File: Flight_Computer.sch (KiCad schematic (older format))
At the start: 138 parts, among them IC1 PIC32MZ2048EFH144-I_PL, IC2 FAN4010IL6X_F113, IC3 FAN4010IL6X_F113, J1 ICSP Programming, J2 SC_19-20, J3 UJ2-MBH-1-SMT-TR, J4 47219-2001, Q1 Q_NPN_BEC, Q2 Q_NPN_BEC, U1 STMPS2141STR, U2 STMPS2141STR, U3 BNO055, U4 SN65HVD1050D, U8 TXB0104PWR

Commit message: More additions
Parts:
- removed C1, C10, C11, C2, C3, C30, C33, C4, C5, C6, C7, C8, C9: 100n, Capacitor_SMD:C_0603_1608Metric, symbol Device:C_Small
- removed C12, C13: 100n, Capacitor_SMD:C_0402_1005Metric, symbol Device:C
- removed C14, C15: 22u, Capacitor_SMD:C_0805_2012Metric, symbol Device:C
- removed C18, C21, C22, C23, C26, C27, C35, C36, C41, C54, C55: 100n, Capacitor_SMD:C_0402_1005Metric, symbol Device:C_Small
- removed C19, C20, C24, C25, C34, C37, C44, C45, C46, C64, C65, C66, C67, C68, C69, C70: 1n, Capacitor_SMD:C_0402_1005Metric, symbol Device:C_Small
- removed C28, C29: 2.2u, Capacitor_SMD:C_0402_1005Metric, symbol Device:C_Small
- removed C31: 1n, Capacitor_SMD:C_0603_1608Metric, symbol Device:C_Small
- removed C32, C39, C40: 100p, Capacitor_SMD:C_0402_1005Metric, symbol Device:C_Small
- removed C47, C48, C49, C60, C61, C62, C63: 10n, Capacitor_SMD:C_0402_1005Metric, symbol Device:C_Small
- removed C50, C51, C52, C56, C57, C58, C59: 1u, Capacitor_SMD:C_0402_1005Metric, symbol Device:C_Small
- removed D1, D2: >8V, Diode_SMD:D_0805_2012Metric, symbol Device:D_TVS
- removed D3: D_TVS_x2_AAC, Package_TO_SOT_SMD:SOT-23, symbol Device:D_TVS_x2_AAC
- removed IC1: PIC32MZ2048EFH144-I_PL, QFP50P2200X2200X160-144N, symbol SamacSys_Parts:PIC32MZ2048EFH144-I_PL
- removed IC2, IC3: FAN4010IL6X_F113, 6-LEAD_MICROPAK, symbol FAN4010IL6X_F113:FAN4010IL6X_F113
- removed J1: ICSP Programming, Connector_PinHeader_2.54mm:PinHeader_1x05_P2.54mm_Vertical, symbol Connector_Generic:Conn_01x05
- removed J2: SC_19-20, MASA_Library:Stack_Connector_2019_2020, symbol MASA_Library:SC_19-20
- removed J3: UJ2-MBH-1-SMT-TR, digikey-footprints:USB_Mini_B_Female_UJ2-MBH-1-SMT-TR, symbol dk_USB-DVI-HDMI-Connectors:UJ2-MBH-1-SMT-TR
- removed J4: 47219-2001, 472192001, symbol MASA_Library:47219-2001
- removed L1: 4.7u, Capacitor_SMD:C_0805_2012Metric, symbol Device:L
- removed L10, L11, L5, L6, L7, L8, L9: 220n, Inductor_SMD:L_0402_1005Metric, symbol Device:L
- removed L2: 4.7u, Inductor_SMD:L_0805_2012Metric, symbol Device:L
- removed L3, L4: 2.2u, Inductor_SMD:L_0402_1005Metric, symbol Device:L
- removed Q1, Q2: Q_NPN_BEC, Package_TO_SOT_SMD:SOT-23, symbol Device:Q_NPN_BEC
- removed R1, R2: 100, Resistor_SMD:R_0805_2012Metric, symbol Device:R_Small_US
- removed R10, R9: 1, Resistor_SMD:R_0402_1005Metric, symbol Device:R_Small_US
- removed R11, R13, R14, R22, R23, R24, R28, R29, R30: 3.3, Resistor_SMD:R_0402_1005Metric, symbol Device:R_Small_US
- removed R12, R25: 1k, Resistor_SMD:R_0402_1005Metric, symbol Device:R_Small_US
- removed R15, R16, R18: 0, Resistor_SMD:R_0603_1608Metric, symbol Device:R_Small_US
- removed R17: 10k, Resistor_SMD:R_0603_1608Metric, symbol Device:R_Small_US
- removed R19, R20: 60, Resistor_SMD:R_0603_1608Metric, symbol Device:R_Small_US
- removed R26, R27, R31, R7, R8: 10k, Resistor_SMD:R_0402_1005Metric, symbol Device:R_Small_US
- removed R3: 10k, Resistor_SMD:R_0805_2012Metric, symbol Device:R_Small_US
- removed R32, R33: 3.3k, Resistor_SMD:R_0402_1005Metric, symbol Device:R_Small_US
- removed R34, R35: 220m, Resistor_SMD:R_0805_2012Metric, symbol Device:R_Small_US
- removed R4: 1k, Resistor_SMD:R_0805_2012Metric, symbol Device:R_Small_US
- removed R5, R6: NP, Resistor_SMD:R_0402_1005Metric, symbol Device:R_Small_US
- removed TMP1, TMP2: LM50CIM3X, Package_TO_SOT_SMD:SOT-23, symbol MASA_Library:LM50CIM3X
- removed TP1, TP10, TP2, TP3, TP4, TP5, TP6, TP7, TP8, TP9: T, TestPoint:TestPoint_Pad_1.0x1.0mm, symbol Connector:TestPoint
- removed U1, U2: STMPS2141STR, digikey-footprints:SOT-753, symbol dk_PMIC-Power-Distribution-Switches-Load-Drivers:STMPS2141STR
- removed U3: BNO055, digikey-footprints:LGA-28_5.2x3.8mm_BNO0055, symbol dk_Motion-Sensors-IMUs-Inertial-Measurement-Units:BNO055
- removed U4: SN65HVD1050D, Package_SO:SOIC-8_3.9x4.9mm_P1.27mm, symbol Interface_CAN_LIN:SN65HVD1050D
- removed U8: TXB0104PWR, digikey-footprints:TSSOP-14_W4.4mm, symbol dk_Logic-Translators-Level-Shifters:TXB0104PWR
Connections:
- net labels removed: !ENABLE_3V3, !ENABLE_5V, +3.3V, +3.3VP, +3V3, +5V, +5VP, 3V3_FAULT, 5V_FAULT, BNO_BL_IND, BNO_BL_LOAD, BNO_ENABLE, BNO_INT, BNO_RX, BNO_TX, CAN_H, CAN_L, CAN_RX, CAN_TX, GND, I_3V3, I_5V, MCLR, PGEC, PGED, SCK, SDI, SDI1, SDO, SD_CLK, SD_CS, SD_MISO, SD_MOSI, TCK, TDI, TDO, TMS, TSENSE_1, TSENSE_2, UART1_RX, UART1_TX, UART2_RX, UART2_TX, USB_3V3, USB_D+, USB_D-, USB_VBUS, VDD
- wire segments 342 -> 0
- no-connect marks 8 -> 0
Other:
- note removed: "Consider Seperating Analog and Digital Grounds / Voltages\n"
- note removed: "ENABLE_X are Active Low\n"
- note removed: "KEEP CLOSE TO PIC PINS"
- note removed: "Power Conditioning"
- note removed: "RX"
- note removed: "TX"
- note removed: "Use high ESR for polarized cap"

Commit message: Finished routing
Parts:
- added C1, C10, C11, C18, C2, C21, C22, C23, C26, C27, C3, C30, C33, C35, C36, C4, C41, C5, C54, C55, C6, C7, C8, C9: 100n, Capacitor_SMD:C_0402_1005Metric, symbol Device:C_Small
- added C12, C13: 100n, Capacitor_SMD:C_0402_1005Metric, symbol Device:C
- added C14, C15: 22u, Capacitor_SMD:C_0805_2012Metric, symbol Device:C
- added C19, C20, C24, C25, C31, C34, C37, C44, C45, C46, C64, C65, C66, C67, C68, C69, C70: 1n, Capacitor_SMD:C_0402_1005Metric, symbol Device:C_Small
- added C28, C29: 2.2u, Capacitor_SMD:C_0402_1005Metric, symbol Device:C_Small
- added C32, C39, C40: 100p, Capacitor_SMD:C_0402_1005Metric, symbol Device:C_Small
- added C47, C48, C49, C60, C61, C62, C63: 10n, Capacitor_SMD:C_0402_1005Metric, symbol Device:C_Small
- added C50, C51, C52, C56, C57, C58, C59: 1u, Capacitor_SMD:C_0402_1005Metric, symbol Device:C_Small
- added D1, D2: >8V, Diode_SMD:D_0805_2012Metric, symbol Device:D_TVS
- added D3: D_TVS_x2_AAC, Package_TO_SOT_SMD:SOT-23, symbol Device:D_TVS_x2_AAC
- added IC1: PIC32MZ2048EFH144-I_PL, QFP50P2200X2200X160-144N, symbol SamacSys_Parts:PIC32MZ2048EFH144-I_PL
- added IC2, IC3: FAN4010IL6X_F113, 6-LEAD_MICROPAK, symbol FAN4010IL6X_F113:FAN4010IL6X_F113
- added J1: ICSP Programming, Connector_PinHeader_2.54mm:PinHeader_1x05_P2.54mm_Vertical, symbol Connector_Generic:Conn_01x05
- added J2: SC_19-20, MASA_Library:Stack_Connector_2019_2020, symbol MASA_Library:SC_19-20
- added J3: UJ2-MBH-1-SMT-TR, digikey-footprints:USB_Mini_B_Female_UJ2-MBH-1-SMT-TR, symbol dk_USB-DVI-HDMI-Connectors:UJ2-MBH-1-SMT-TR
- added J4: 47219-2001, 472192001, symbol MASA_Library:47219-2001
- added L1: 4.7u, Capacitor_SMD:C_0805_2012Metric, symbol Device:L
- added L10, L11, L5, L6, L7, L8, L9: 220n, Inductor_SMD:L_0402_1005Metric, symbol Device:L
- added L2: 4.7u, Inductor_SMD:L_0805_2012Metric, symbol Device:L
- added L3, L4: 2.2u, Inductor_SMD:L_0402_1005Metric, symbol Device:L
- added Q1, Q2: Q_NPN_BEC, Package_TO_SOT_SMD:SOT-23, symbol Device:Q_NPN_BEC
- added R1, R2: 100, Resistor_SMD:R_0402_1005Metric, symbol Device:R_Small_US
- added R10, R9: 1, Resistor_SMD:R_0402_1005Metric, symbol Device:R_Small_US
- added R11, R13, R14, R22, R23, R24, R28, R29, R30: 3.3, Resistor_SMD:R_0402_1005Metric, symbol Device:R_Small_US
- added R12, R25, R4: 1k, Resistor_SMD:R_0402_1005Metric, symbol Device:R_Small_US
- added R15, R16, R18: 0, Resistor_SMD:R_0402_1005Metric, symbol Device:R_Small_US
- added R17, R26, R27, R3, R31, R7, R8: 10k, Resistor_SMD:R_0402_1005Metric, symbol Device:R_Small_US
- added R19, R20: 60, Resistor_SMD:R_0603_1608Metric, symbol Device:R_Small_US
- added R21, R32, R33, R36: 3.3k, Resistor_SMD:R_0402_1005Metric, symbol Device:R_Small_US
- added R34, R35: 220m, Resistor_SMD:R_0805_2012Metric, symbol Device:R_Small_US
- added R5, R6: NP, Resistor_SMD:R_0402_1005Metric, symbol Device:R_Small_US
- added TMP1, TMP2: LM50CIM3X, Package_TO_SOT_SMD:SOT-23, symbol MASA_Library:LM50CIM3X
- added TP1, TP10, TP2, TP3, TP4, TP5, TP6, TP7, TP8, TP9: T, TestPoint:TestPoint_Pad_1.0x1.0mm, symbol Connector:TestPoint
- added U1, U2: STMPS2141STR, digikey-footprints:SOT-753, symbol dk_PMIC-Power-Distribution-Switches-Load-Drivers:STMPS2141STR
- added U3: BNO055, digikey-footprints:LGA-28_5.2x3.8mm_BNO0055, symbol dk_Motion-Sensors-IMUs-Inertial-Measurement-Units:BNO055
- added U4: SN65HVD1050D, Package_SO:SOIC-8_3.9x4.9mm_P1.27mm, symbol Interface_CAN_LIN:SN65HVD1050D
- added U8: TXB0104PWR, digikey-footprints:TSSOP-14_W4.4mm, symbol dk_Logic-Translators-Level-Shifters:TXB0104PWR
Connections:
- new net: J1.4 (Pin_4), R1.2
- new net: J1.5 (Pin_5), R2.1
- new net: C2.2, R3.1, R4.2, TP1.1
- new net: C13.1, D2.2 (A2), L2.1, TP4.1, U2.1 (OUT)
- new net: R6.2, R8.2, U2.4 (EN)
- new net: C12.1, D1.2 (A2), L1.1, TP3.1, U1.1 (OUT)
- new net: C14.1, IC2.1 (VIN), L1.2, R34.1, TP5.1
- new net: C14.2, R9.2
- new net: R5.2, R7.2, U1.4 (EN)
- new net: C15.2, R10.2
- new net: Q2.3 (C), R27.1, U3.11 (RESET)
- new net: U3.19 (COM1), U8.13 (B1)
- new net: U3.20 (COM0), U8.12 (B2)
- new net: Q1.3 (C), R26.1, U3.4 (BOOT_LOAD)
- new net: C33.1, U3.9 (CAP)
- new net: C15.1, IC3.1 (VIN), L2.2, R35.1, TP6.1
- new net: C56.2, C60.2, J2.25 (UART1_TX), L8.2
- new net: C65.2, J2.27 (UART1_RX), L9.1
- new net: C58.2, C62.2, J2.29 (UART2_TX), L10.2
- new net: C67.2, J2.31 (UART2_RX), L11.1
- new net: C32.2, R15.2, U4.1 (TXD)
- new net: R16.2, U4.4 (RXD)
- new net: R18.1, U4.5 (VREF)
- new net: R17.2, U4.8 (S)
- new net: C22.2, C24.2, L3.1, R21.2, TMP1.2 (Vout)
- new net: C41.2, R18.2, R19.2, R20.1
- new net: C29.1, R14.1
- new net: C23.2, C25.2, L4.1, R36.2, TMP2.2 (Vout)
- new net: C50.1, R22.1
- new net: C51.1, R23.1
- new net: C52.1, R24.1
- new net: C54.1, Q1.1 (B), R12.1
- new net: C55.1, Q2.1 (B), R25.1
- new net: C28.1, R13.1
- new net: C56.1, R11.1
- new net: C57.1, R28.1
- new net: C58.1, R29.1
- new net: C59.1, R30.1
- new net !ENABLE_3V3: R5.1
- new net !ENABLE_5V: R6.1
- new net +3.3VP: J2.2 (3V3), J2.3 (3V3), J2.6 (3V3), J2.7 (3V3), U1.5 (IN)
- new net +3V3: C1.1, C10.2, C11.2, C3.1, C36.2, C37.2, C4.1, C5.1, C6.1, C69.2, C7.1, C8.1, C9.1, IC1.107 (VDD_6), IC1.122 (VDD_7), IC1.137 (VDD_8), IC1.18 (VDD_1), IC1.33 (VDD_2), IC1.41 (AVDD), IC1.55 (VDD_3), IC1.64 (VDD_4), IC1.88 (VDD_5), IC2.6 (LOAD), J1.2 (Pin_2), J4.4 (VDD), R3.2, R34.2, U8.1 (VCCA)
- new net +5V: C18.2, C19.1, C20.2, C21.1, C30.1, C31.1, C34.2, C35.2, C68.1, C70.1, IC3.6 (LOAD), R26.2, R27.2, R31.2, R35.2, TMP1.1 (Vs), TMP2.1 (Vs), U3.28 (VDDIO), U3.3 (VDD), U3.5 (PS1), U4.3 (VCC), U8.14 (VCCB), U8.8 (OE)
- new net +5VP: J2.34 (5V0), J2.35 (5V0), J2.38 (5V0), J2.39 (5V0), U2.5 (IN)
- new net 3V3_FAULT: U1.3 (FAULT)
- new net 5V_FAULT: U2.3 (FAULT)
- new net BNO_BL_IND: IC1.102 (RH14), U3.10 (BL_IND)
- new net BNO_BL_LOAD: IC1.101 (ERXDV/ECRSDV/RH13), R12.2
- new net BNO_ENABLE: IC1.100 (ECRS/RH12), R25.2
- new net BNO_INT: IC1.103 (EBIA23/RH15), U3.14 (INT)
- new net BNO_RX: IC1.91 (EBIA8/RPF5/SCL5/PMA8/RF5), U8.3 (A2)
- new net BNO_TX: IC1.90 (EBIA9/RPF4/SDA5/PMA9/RF4), U8.2 (A1)
- new net CAN_H: C39.2, D3.1 (A1), J2.21 (CAN_H), R19.1, TP9.1, U4.7 (CANH)
- new net CAN_L: C40.1, D3.2 (A2), J2.23 (CAN_L), R20.2, TP10.1, U4.6 (CANL)
- new net CAN_RX: IC1.105 (SOSCI/RPC13/RC13), R16.1, TP8.1
- new net CAN_TX: IC1.106 (SOSCO/RPC14/T1CK/RC14), R15.1, TP7.1
- new net GND: C1.2, C10.1, C11.1, C12.2, C13.2, C18.1, C19.2, C2.1, C20.1, C21.2, C22.1, C23.1, C24.1, C25.1, C26.1, C27.1, C3.2, C30.2, C31.2, C32.1, C33.2, C34.1, C35.1, C36.1, C37.1, C39.1, C4.2, C40.2, C41.1, C44.1, C45.1, C46.1, C47.1, C48.1, C49.1, C5.2, C54.2, C55.2, C6.2, C60.1, C61.1, C62.1, C63.1, C64.1, C65.1, C66.1, C67.1, C68.2, C69.1, C7.2, C70.2, C8.2, C9.2, D1.1 (A1), D2.1 (A1), D3.3 (common), IC1.108 (VSS_7), IC1.123 (VSS_8), IC1.136 (VSS_9), IC1.17 (VSS_1), IC1.32 (VSS_2), IC1.42 (AVSS), IC1.54 (VSS_3), IC1.63 (VSS_4), IC1.75 (VSS_5), IC1.89 (VSS_6), IC2.5 (GND), IC3.5 (GND), J1.3 (Pin_3), J2.1 (GND), J2.19 (GND), J2.20 (GND), J2.36 (GND), J2.37 (GND), J2.4 (GND), J2.40 (GND), J2.5 (GND), J3.5, J3.SH, J4.10 (GND_2), J4.11 (GND_3), J4.12 (GND_4), J4.6 (VSS), J4.9 (GND_1), Q1.2 (E), Q2.2 (E), R10.1, R11.2, R13.2, R14.2, R17.1, R21.1, R22.2, R23.2, R24.2, R28.2, R29.2, R30.2, R31.1, R32.1, R33.1, R36.1, R7.1, R8.1, R9.1, TMP1.3 (GND), TMP2.3 (GND), U1.2 (GND), U2.2 (GND), U3.15 (PIN15), U3.16 (PIN16), U3.17 (COM3), U3.18 (COM2), U3.2 (GND), U3.25 (GNDIO), U3.6 (PS0), U4.2 (GND), U8.7 (GND)
- new net I_3V3: IC1.66 (AN41/ERXD1/RH5), IC2.3 (IOUT), R32.2
- new net I_5V: IC1.65 (AN40/ERXERR/RH4), IC3.3 (IOUT), R33.2
- new net MCLR: IC1.20 (~MCLR), J1.1 (Pin_1), R4.1, TP2.1
- new net PGEC: IC1.35 (PGEC1/AN1/RPB1/RB1), R2.2
- new net PGED: IC1.36 (PGED1/AN0/RPB0/RB0), R1.1
- new net SCK: C46.2, IC1.109 (RPD1/SCK1/RD1), L7.1
- new net SDI: C48.2, C51.2, IC1.120 (ETXEN/RPD6/RD6), L6.2
- new net SDO: C44.2, IC1.110 (EBID14/RPD2/PMD14/RD2), L5.1
- new net SD_CLK: C49.2, C52.2, J4.5 (CLK), L7.2
- new net SD_CS: J4.2 (CD/DAT3)
- new net SD_MISO: C45.2, J4.7 (DAT0), L6.1
- new net SD_MOSI: C47.2, C50.2, J4.3 (CMD), L5.2
- new net TCK: IC1.56 (TCK/AN29/RA1)
- new net TDI: IC1.57 (TDI/AN30/RPF13/SCK5/RF13)
- new net TDO: IC1.58 (TDO/AN31/RPF12/RF12)
- new net TSENSE_1: C26.2, C28.2, IC1.49 (CVREFOUT/AN5/RPB10/RB10), L3.2
- new net TSENSE_2: C27.2, C29.2, IC1.50 (AN6/RB11), L4.2
- new net UART1_RX: C57.2, C61.2, IC1.118 (~SQICS0~/RPD4/RD4), L9.2
- new net UART1_TX: C64.2, IC1.119 (~SQICS1~/RPD5/RD5), L8.1
- new net UART2_RX: C59.2, C63.2, IC1.128 (EBID8/RPG0/PMD8/RG0), L11.2
- new net UART2_TX: C66.2, IC1.127 (EBID9/RPG1/PMD9/RG1), L10.1
- new net USB_3V3: IC1.74 (VUSB3V3)
- new net USB_D+: IC1.77 (D+), J3.3
- new net USB_D-: IC1.76 (D-), J3.2
- new net USB_VBUS: IC1.73 (VBUS), J3.1
- no-connect marks 0 -> 8
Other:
- note added: "Consider Seperating Analog and Digital Grounds / Voltages\n"
- note added: "ENABLE_X are Active Low\n"
- note added: "KEEP CLOSE TO PIC PINS"
- note added: "Power Conditioning"
- note added: "RX"
- note added: "TX"
- note added: "Use high ESR for polarized cap"

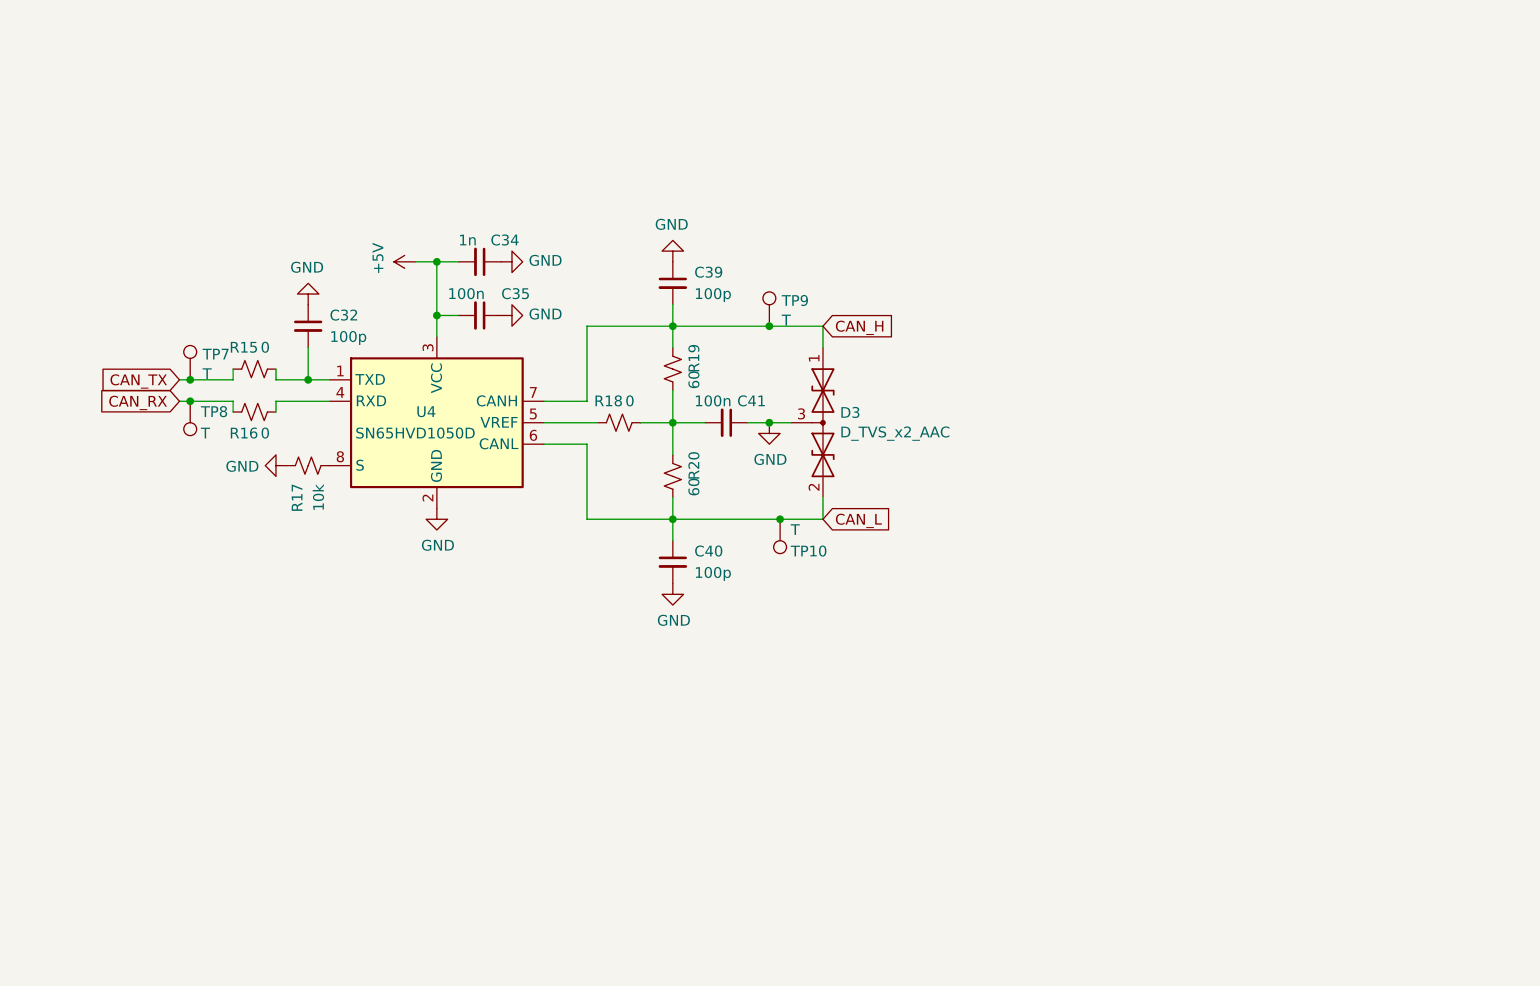
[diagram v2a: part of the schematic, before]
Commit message: Fixed CAN Bus voltage error
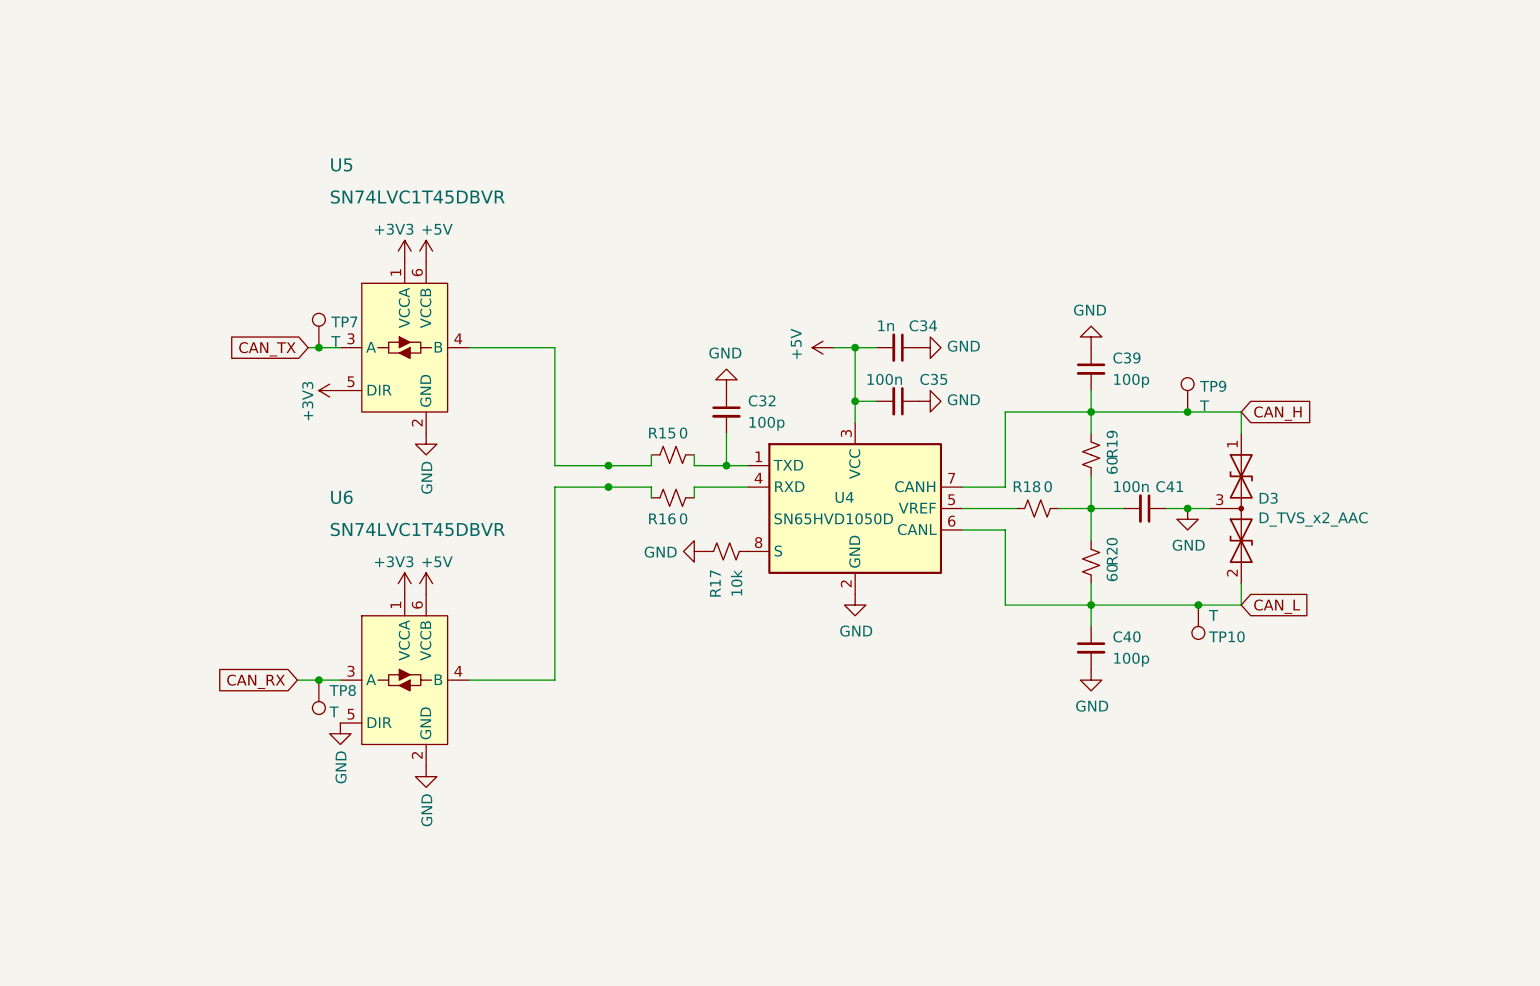
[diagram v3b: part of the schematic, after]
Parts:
- added U5, U6: SN74LVC1T45DBVR, digikey-footprints:SOT-23-6, symbol dk_Logic-Translators-Level-Shifters:SN74LVC1T45DBVR
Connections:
- net +3V3: now also U5.1 (VCCA), U5.5 (DIR), U6.1 (VCCA)
- net +5V: now also U5.6 (VCCB), U6.6 (VCCB)
- net CAN_RX: now also U6.3 (A); no longer R16.1
- net CAN_TX: now also U5.3 (A); no longer R15.1
- net GND: now also U5.2 (GND), U6.2 (GND), U6.5 (DIR)
- new net: R15.1, U5.4 (B)
- new net: R16.1, U6.4 (B)
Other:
- moved on the sheet: C32, C34, C35, C39, C40, C41, D3, R15, R16, R17, R18, R19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

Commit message: Gerbers added
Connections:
- net SD_CS: now also IC1.114 (ETXERR/RJ0)
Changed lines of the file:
@@
 	1    0    0    -1
 $EndComp
-Connection ~ 3650 7550
-Wire Wire Line
-	3650 7550 3850 7550
 $Comp
 L Connector:TestPoint TP8
@@
 	-1   0    0    1
 $EndComp
-Connection ~ 3650 7650
-Wire Wire Line
-	3650 7650 3850 7650
 $Comp
 L Connector:TestPoint TP5
@@
 	3400 7000 3400 7550
 Wire Wire Line
-	3400 7550 3650 7550
-Wire Wire Line
 	3000 8550 3400 8550
 Wire Wire Line
 	3400 8550 3400 7650
-Wire Wire Line
-	3400 7650 3650 7650
 Wire Wire Line
 	2250 7000 2300 7000
@@
 Wire Wire Line
 	2300 7000 2400 7000
+Wire Wire Line
+	3400 7550 3850 7550
+Wire Wire Line
+	3400 7650 3850 7650
+Text GLabel 7650 12850 1    50   Input ~ 0
+SD_CS
 $EndSCHEMATC

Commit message: Major changes to routing and fixed filters
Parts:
- removed C50, C51, C52, C56, C57, C58, C59: 1u, Capacitor_SMD:C_0402_1005Metric, symbol Device:C_Small
- added C16, C17: 1n, Capacitor_SMD:C_0402_1005Metric, symbol Device:C_Small
- added R37, R38: 470, Resistor_SMD:R_0402_1005Metric, symbol Device:R_Small_US
- added TP11, TP12, TP13, TP14, TP15, TP16: T, TestPoint:TestPoint_Pad_D1.0mm, symbol Connector:TestPoint
- C44, C45, C46: value 1n -> 330p
- C47, C48, C49, C60, C61, C62, C63: value 10n -> NP
- L10, L11, L5, L6, L7, L8, L9: value 220n -> 0
- R11, R22, R23, R24, R28, R29, R30: value 3.3 -> 470
- R21, R36: value 3.3k -> NP
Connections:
- net BNO_RX: now also R37.1; no longer U8.3 (A2)
- net BNO_TX: now also C16.2, R38.2; no longer U8.2 (A1)
- net GND: now also C16.1, C17.1; no longer R11.2, R22.2, R23.2, R24.2, R28.2, R29.2, R30.2
- net SCK: now also R24.1, TP13.1; no longer C46.2, L7.1
- net SDI: now also TP15.1
- net SDO: now also R22.1, TP11.1; no longer C44.2, L5.1
- net SD_CLK: now also TP16.1
- net SD_MISO: now also R23.1, TP12.1; no longer C45.2, L6.1
- net SD_MOSI: now also TP14.1
- net UART1_TX: now also R28.1; no longer C64.2, L8.1
- net UART2_TX: now also R11.1; no longer C66.2, L10.1
- net at C65.2, L9.1: now also R29.1; no longer J2.27 (UART1_RX)
- net at C67.2, L11.1: now also R30.1; no longer J2.31 (UART2_RX)
- new net: J2.27 (UART1_RX), R29.2
- new net: J2.31 (UART2_RX), R30.2
- new net: C44.2, L5.1, R22.2
- new net: C45.2, L6.1, R23.2
- new net: C46.2, L7.1, R24.2
- new net: R38.1, U8.2 (A1)
- new net: C17.2, R37.2, U8.3 (A2)
- new net: C64.2, L8.1, R28.2
- new net: C66.2, L10.1, R11.2
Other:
- moved on the sheet: C60, C61, C62, C63, C64, C65, C66, C67, L10, L11, L8, L9
